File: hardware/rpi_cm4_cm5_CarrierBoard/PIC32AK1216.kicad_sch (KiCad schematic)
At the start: 92 parts, among them J10 PR20206VBNN, Q21 2N7002, Q25 2N7002, Q26 2N7002, U1 PIC32AK1216GC41064-I/M7, U20 STWD100NYWY3F, Y3 20MHz

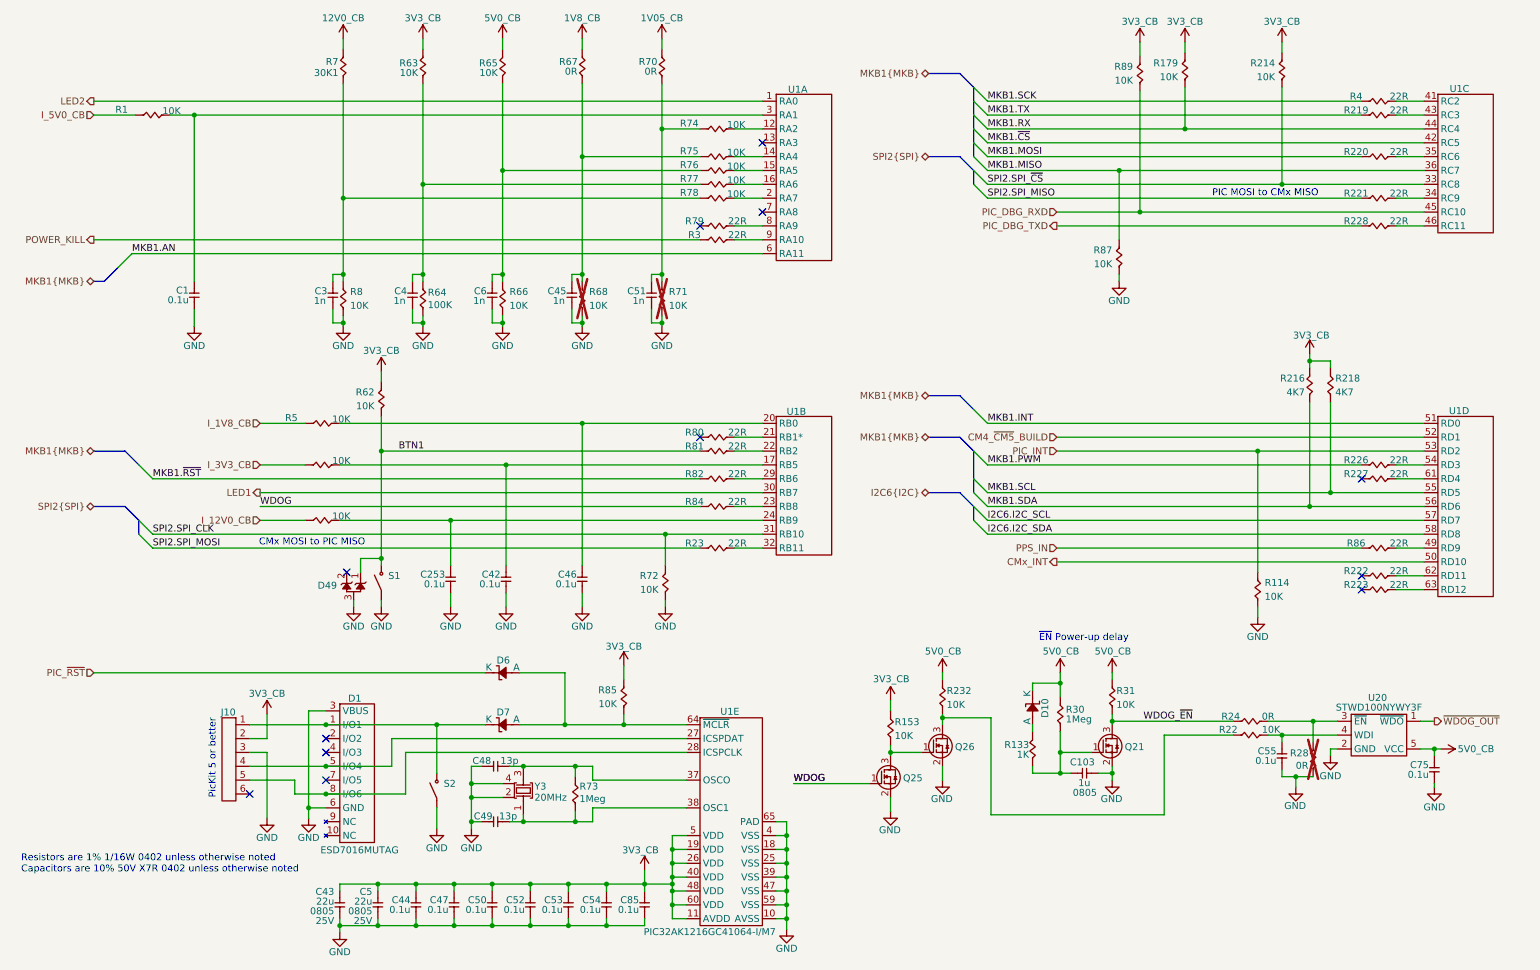
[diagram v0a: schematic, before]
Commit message: Add test points on relevant signals Re-generate SCH_PDF Re-generate BOM Re-generate all gerbers and relevant PCB output files (still in review phase)
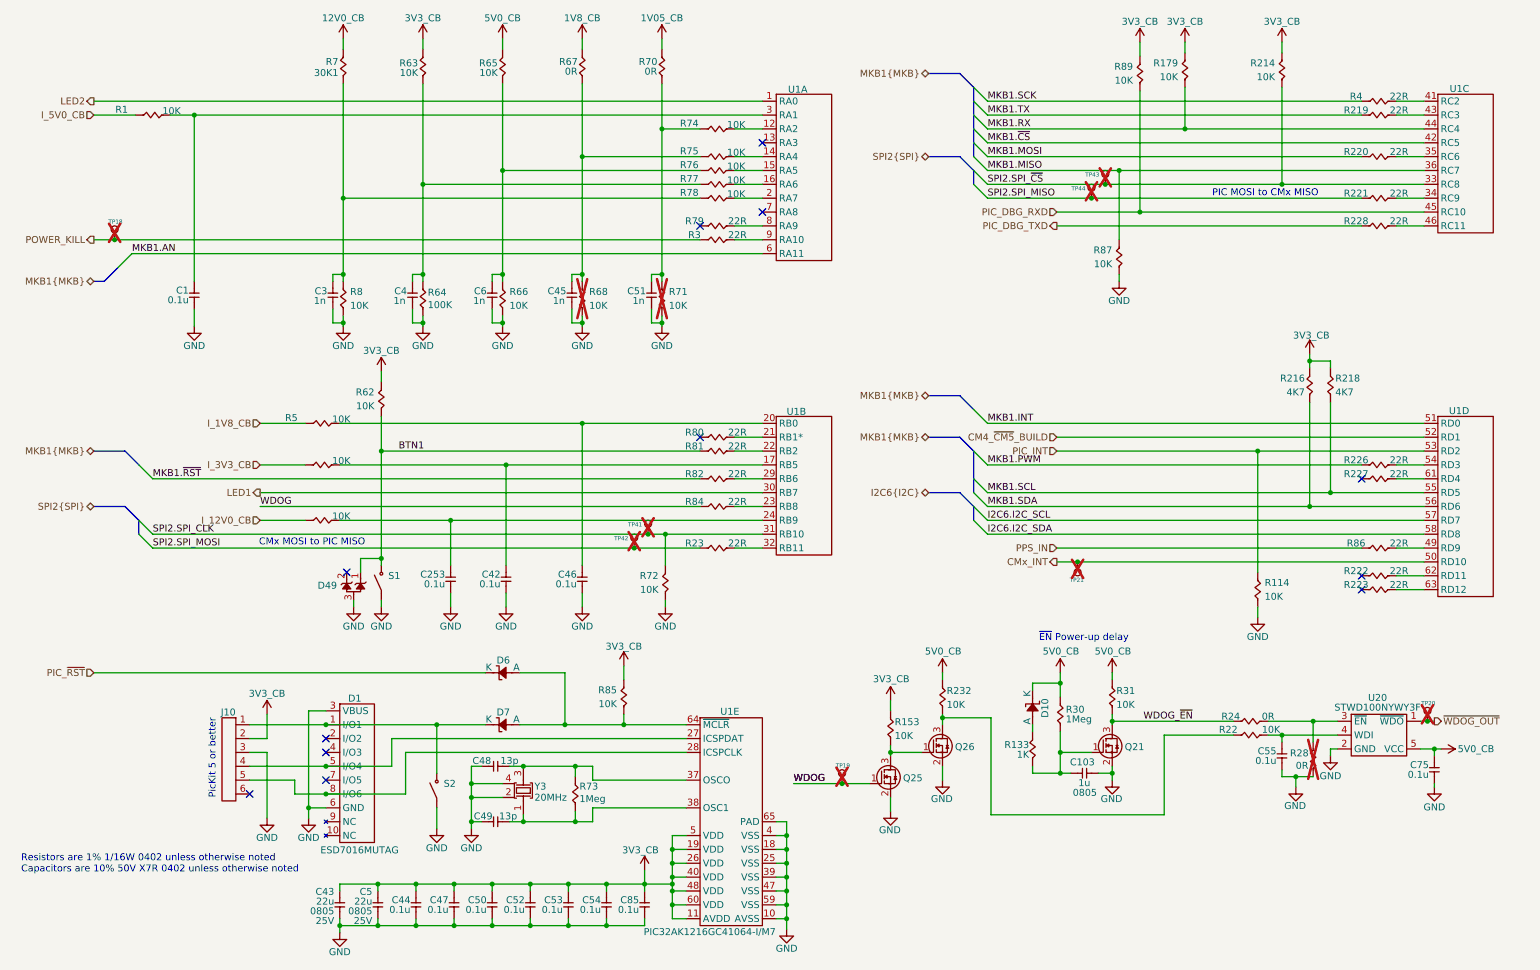
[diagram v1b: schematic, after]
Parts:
- added TP18, TP19, TP20, TP21, TP41, TP42, TP43, TP44: 28 mils, footprint:SMT_TP_28_MILS, symbol KicadCompDb:Test Point/TP_00001
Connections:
- net CMx_INT: now also TP21.1
- net POWER_KILL: now also TP18.1
- net SPI2.SPI_CLK: now also TP41.1
- net SPI2.SPI_MISO: now also TP44.1
- net SPI2.SPI_MOSI: now also TP42.1
- net SPI2.SPI_~{CS}: now also TP43.1
- net WDOG: now also TP19.1
- net ~{WDOG_OUT}: now also TP20.1

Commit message: Final commit prior to formal DFM by PCB manufacturer & PCBA Several iterations of DRC checks and validation with CAM software completed Ready for quotation
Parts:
- S1, S2: value Y35A23310FPLFG -> KSR233G LFG; Manufacturer Part Number Y35A23310FPLFG -> KSR233G LFG
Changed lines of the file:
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@@
 	(title_block
 		(title "RPI CMx Carrier")
-		(date "2026-02-24")
+		(date "2026-02-26")
 		(rev "2.00-0A")
 		(comment 1 "Jean-Francois Bilodeau")
@@
 			)
 		)
-		(property "Value" "Y35A23310FPLFG"
+		(property "Value" "KSR233G LFG"
 			(at 80.01 120.6499 90)
 			(effects
@@
 			)
 		)
-		(property "Manufacturer Part Number" "Y35A23310FPLFG"
+		(property "Manufacturer Part Number" "KSR233G LFG"
 			(at 86.614 121.031 0)
 			(effects
@@
 			)
 		)
-		(property "Value" "Y35A23310FPLFG"
+		(property "Value" "KSR233G LFG"
 			(at 90.17 158.7499 90)
 			(effects
@@
 			)
 		)
-		(property "Manufacturer Part Number" "Y35A23310FPLFG"
+		(property "Manufacturer Part Number" "KSR233G LFG"
 			(at 96.774 159.131 0)
 			(effects
